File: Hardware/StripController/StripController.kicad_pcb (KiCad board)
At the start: 2 copper layers, 39.6 x 48.3 mm, 49 parts, among them IC1 RY8310, IC2 CH32V003F4U6, J1 Conn_01x03_Socket, J2 Conn_01x06_Socket, J4 Conn_01x02_Pin, J5 TagConnect, J6 Conn_01x03_Socket, Q1 AON7544, Q2 AON7544, Q3 AON7544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

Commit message: edit pcb desine
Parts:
- added C12: 100n, Capacitor_SMD:C_0402_1005Metric, F.Cu at (156.7, 75.7)
- added C13: 100n, Capacitor_SMD:C_0402_1005Metric, F.Cu at (137.8, 59.8)
- added F2: 0,2A, Fuse:Fuse_0402_1005Metric, F.Cu at (155.7, 93.2)
- added R14: 10k, Resistor_SMD:R_0402_1005Metric, F.Cu at (137.2, 93.4)
- added R14: R, Resistor_SMD:R_0402_1005Metric, F.Cu at (155.7, 75.6)
- added R15: 10k, Resistor_SMD:R_0402_1005Metric, F.Cu at (137.1, 86.3)
- added R16: 0, Resistor_SMD:R_0402_1005Metric, B.Cu at (149.9, 98.6)
- added R17: 0, Resistor_SMD:R_0402_1005Metric, B.Cu at (149.9, 100.6)
- added R18: R, Resistor_SMD:R_0402_1005Metric, F.Cu at (156.7, 73.6)
- added R19: 100k, Resistor_SMD:R_0402_1005Metric, F.Cu at (137.8, 57.3)
- added TH1: Thermistor_NTC, Resistor_SMD:R_0402_1005Metric, F.Cu at (137.8, 58.6)
- F1: value Fuse -> 10A
- Q1, Q2, Q3, Q4, Q5: footprint Package_DFN_QFN:DFN-8-1EP_3x3mm_P0.5mm_EP1.65x2.38mm_ThermalVias -> Techbeard:AON7544
- R1: moved to B.Cu
- R7: value NC -> 1k; moved to B.Cu
- moved D4 72.1 mm to (160.8, 50.1), turned to -90 degrees
- moved D3 70.0 mm to (158.8, 50.1), turned to -90 degrees
- moved R13 69.7 mm to (160.8, 52.3), turned to 90 degrees
- moved D2 67.9 mm to (156.8, 50.1), turned to -90 degrees
- moved R12 67.5 mm to (158.8, 52.3), turned to 90 degrees
- moved R1 66.8 mm to (154.7, 99.6)
- moved C6 66.0 mm to (150.0, 78.2), turned to -90 degrees
- moved R11 65.4 mm to (156.8, 52.3), turned to 90 degrees
- moved Q2 65.2 mm to (160.5, 77.2)
- moved R8 64.8 mm to (156.7, 77.7)
- moved C10 64.3 mm to (148.1, 65.1), turned to -90 degrees
- moved R7 62.1 mm to (144.3, 99.6)
- moved C11 62.0 mm to (146.1, 65.1), turned to -90 degrees
- moved D1 60.0 mm to (152.1, 83.3)
- moved R6 59.6 mm to (157.7, 73.7), turned to 90 degrees
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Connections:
- D3 pad 1: StateLed0 -> StateLed1
- D4 pad 1: StateLed1 -> StateLed0
- IC2 pad 10: unconnected-(IC2-PC3-Pad10) -> Voltage
- IC2 pad 11: unconnected-(IC2-PC4-Pad11) -> U2_DE
- IC2 pad 12: unconnected-(IC2-PC5-Pad12) -> U2_RE
- IC2 pad 16: unconnected-(IC2-PD2-Pad16) -> Temp
- IC2 pad 20: U4_RO -> U2_RO
- Q2 pad 4: R -> B
- Q3 pad 4: G -> R
- Q4 pad 4: B -> G
- Q6 pad 3: VCC -> Net-(Q6-D)
- R6 pad 2: G -> R
- R8 pad 2: R -> B
- R9 pad 2: B -> G
- U2 pad 2: +5V -> U2_RE
- U2 pad 3: +5V -> U2_DE
- U4 pad 1: U4_RO -> U2_RO
- U4 pad 2: GND -> Net-(U4-DE)
- U4 pad 3: GND -> Net-(U4-DE)
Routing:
- net +5V: track 0.00 -> 107.8 mm
- net U2_DE: track 0.00 -> 51.6 mm, vias 0 -> 2
- net U2_RE: track 0.00 -> 44.4 mm, vias 0 -> 2
- net U2_DI: track 0.00 -> 43.4 mm, vias 0 -> 2
- net U2_RO: track 0.00 -> 39.9 mm, vias 0 -> 3
- net R: track 0.00 -> 25.7 mm
- net NRST: track 0.00 -> 24.2 mm
- net B: track 0.00 -> 23.9 mm
- net Voltage: track 0.00 -> 22.0 mm
- net RB: track 0.00 -> 21.6 mm
- net G: track 0.00 -> 21.5 mm
- net W: track 0.00 -> 20.8 mm
- net RA: track 0.00 -> 20.0 mm
- net StateLed0: track 0.00 -> 19.9 mm, vias 0 -> 2
- net TB: track 0.00 -> 19.5 mm
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- added copper zone on F.Cu, net +5V
- added copper zone on F.Cu, net B_OUT
- added copper zone on B.Cu, net GND
- added copper zone on F.Cu, net GND
- added copper zone on F.Cu, net Net-(D1-K)
- added copper zone on F.Cu, net Net-(IC1-SW)
- added copper zone on F.Cu, net Net-(J4-Pin_1)
- added copper zone on F.Cu, net R_OUT
- added copper zone on F.Cu, net VCC
- added copper zone on F.Cu, net WW_OUT
- added copper zone on F.Cu, net W_OUT
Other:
- board size 39.6 x 48.3 mm -> 40 x 60 mm

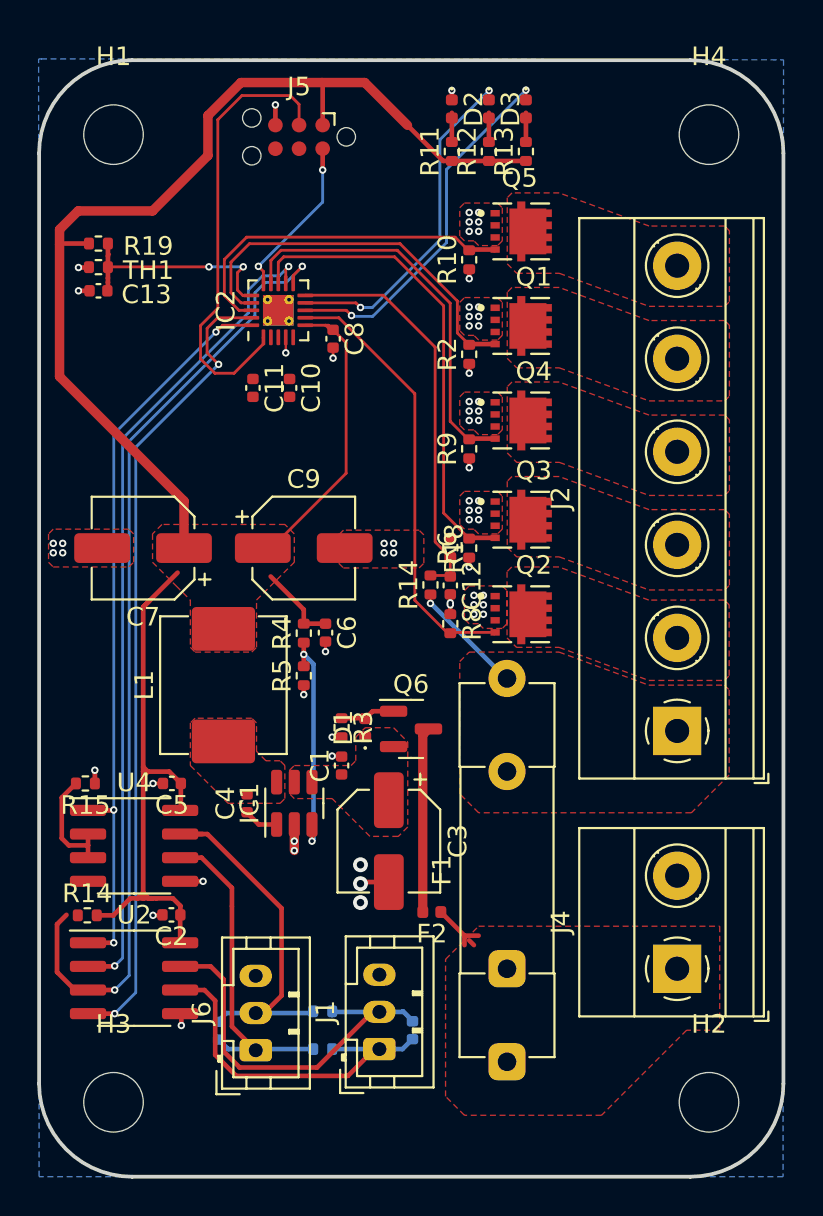
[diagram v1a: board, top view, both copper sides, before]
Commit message: edit Strip controller and buy first batch
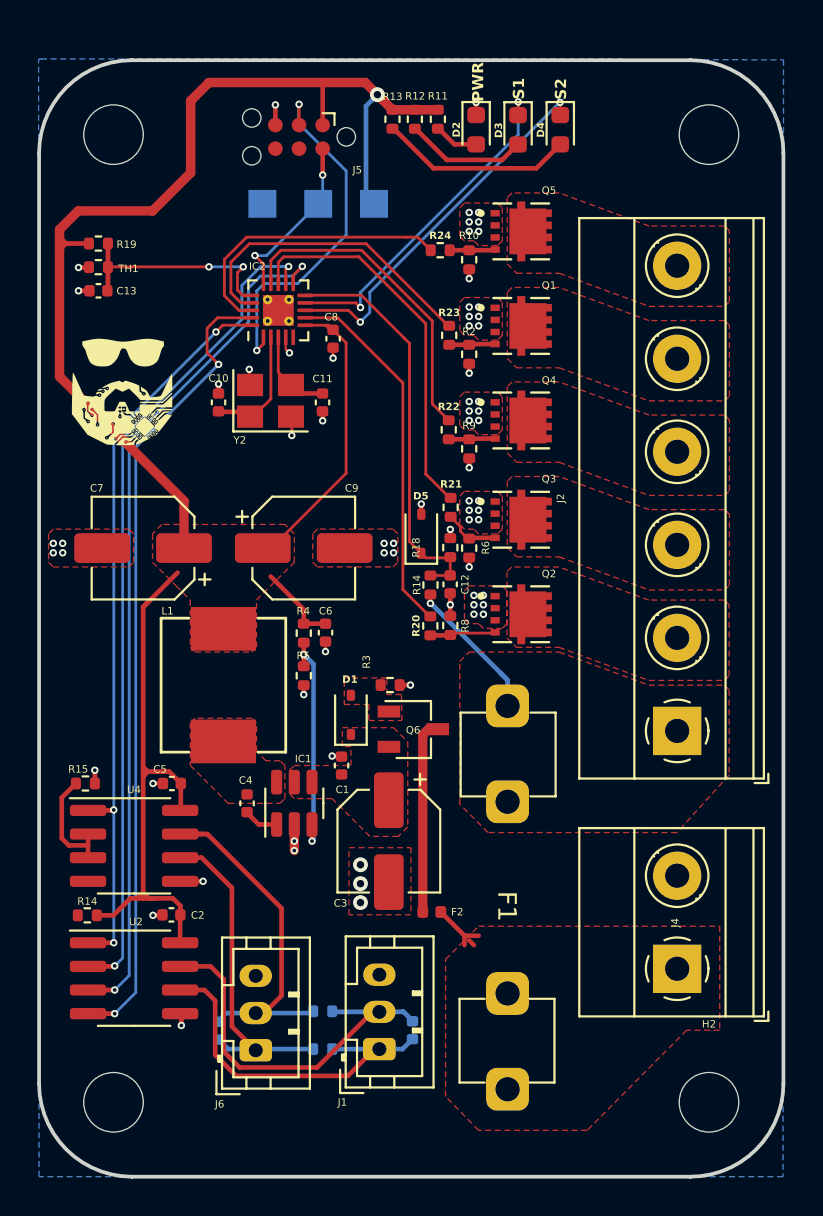
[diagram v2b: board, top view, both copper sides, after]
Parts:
- removed F1: 10A, Fuse:Fuseholder_Clip-5x20mm_Schurter_CQM_Inline_P20.60x5.00mm_D1.00mm_Horizontal
- added D5: 5,1V, Diode_SMD:D_SOD-323, F.Cu at (155.2, 72.9)
- added G***: LOGO, Techbeard:Techbeard_6x6, F.Cu at (139.1, 65.1)
- added G***: LOGO, LOGO, B.Cu at (138.3, 77.4)
- added J10: F1, Techbeard:Fuseholder C3130, F.Cu at (159.8, 84.7)
- added J3: SWD, TestPoint:TestPoint_Pad_1.5x1.5mm, B.Cu at (149.6, 55.2)
- added J7: +5V, TestPoint:TestPoint_Pad_1.5x1.5mm, B.Cu at (152.6, 55.2)
- added J8: GND, TestPoint:TestPoint_Pad_1.5x1.5mm, B.Cu at (146.6, 55.2)
- added J9: F1, Techbeard:Fuseholder C3130, F.Cu at (159.8, 100.2)
- added R20: 47, Resistor_SMD:R_0402_1005Metric, F.Cu at (155.6, 77.8)
- added R21: 47, Resistor_SMD:R_0402_1005Metric, F.Cu at (156.7, 71.5)
- added R22: 47, Resistor_SMD:R_0402_1005Metric, F.Cu at (156.6, 67.3)
- added R23: 47, Resistor_SMD:R_0402_1005Metric, F.Cu at (156.7, 62.2)
- added R24: 47, Resistor_SMD:R_0402_1005Metric, F.Cu at (156.2, 57.7)
- added Y2: Crystal_GND24, Crystal:Crystal_SMD_3225-4Pin_3.2x2.5mm, F.Cu at (147.1, 65.7)
- C3: value 47u -> 22u
- D1: footprint Diode_SMD:D_0402_1005Metric -> Diode_SMD:D_SOD-323
- D2: value LED -> PWR; footprint LED_SMD:LED_0402_1005Metric -> LED_SMD:LED_0603_1608Metric
- D3: value LED -> S1; footprint LED_SMD:LED_0402_1005Metric -> LED_SMD:LED_0603_1608Metric
- D4: value LED -> S2; footprint LED_SMD:LED_0402_1005Metric -> LED_SMD:LED_0603_1608Metric
- L1: footprint Inductor_SMD:L_Abracon_ASPI-0630LR -> Techbeard:L_0630
- Q6: footprint Package_TO_SOT_SMD:SOT-23 -> Package_TO_SOT_SMD:TSOT-23
- R14: value R -> 1M
- R18: value R -> 270k
- moved R13 7.38 mm to (153.6, 50.6), turned to -90 degrees
- moved R12 4.34 mm to (154.8, 50.6), turned to -90 degrees
- moved C10 3.90 mm to (144.3, 65.8), turned to 90 degrees
- moved C11 3.82 mm to (149.9, 65.8)
- moved R3 3.47 mm to (153.5, 81.0), turned to 0 degrees
- moved D4 2.16 mm to (162.6, 51.2)
- moved D3 1.93 mm to (160.4, 51.2)
- moved R11 1.89 mm to (156.0, 50.6), turned to -90 degrees
- moved D2 1.72 mm to (158.1, 51.2)
- moved D1 1.03 mm to (151.4, 82.6)
- moved Q6 0.12 mm to (154.7, 83.4)
- moved R8 0.09 mm to (156.7, 77.8)
- moved C12 0.06 mm to (156.7, 75.6)
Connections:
- IC2 pad 13: R -> G
- IC2 pad 14: G -> B
- IC2 pad 2: (no net) -> Net-(IC2-PA1/OSCI)
- IC2 pad 3: (no net) -> Net-(IC2-PA2/OSCO)
- IC2 pad 7: B -> R
- Q1 pad 4: W -> Net-(Q1-G)
- Q2 pad 4: B -> Net-(Q2-G)
- Q3 pad 4: R -> Net-(Q3-G)
- Q4 pad 4: G -> Net-(Q4-G)
- Q5 pad 4: WW -> Net-(Q5-G)
- R10 pad 2: WW -> Net-(Q5-G)
- R2 pad 2: W -> Net-(Q1-G)
- R6 pad 2: R -> Net-(Q3-G)
- R8 pad 2: B -> Net-(Q2-G)
- R9 pad 2: G -> Net-(Q4-G)
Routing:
- net Net-(D4-A): track 1.57 -> 10.4 mm
- net Net-(IC2-PA1/OSCI): track 0.00 -> 6.62 mm
- net B: track 23.9 -> 17.4 mm
- net R: track 25.7 -> 19.8 mm
- net Net-(D3-A): track 1.57 -> 6.58 mm
- net U2_DE: track 51.6 -> 46.6 mm
- net NRST: track 24.2 -> 19.3 mm, vias 0 -> 2
- net Net-(IC2-PA2/OSCO): track 0.00 -> 4.73 mm
- net W: track 20.8 -> 16.9 mm
- net Net-(Q2-G): track 0.00 -> 3.81 mm
- net WW: track 19.1 -> 15.6 mm
- net GND: track 17.0 -> 20.1 mm, vias 64 -> 69
- net Net-(Q3-G): track 0.00 -> 3.04 mm
- net Net-(D1-A): track 2.97 -> 0.00 mm
- net Net-(Q5-G): track 0.00 -> 2.52 mm
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- added copper zone on F.Cu, net G_OUT
- added copper zone on F.Cu, net Net-(D1-A)
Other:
- board text added: "B"
- board text added: "G"
- board text added: "GND"
- board text added: "R"
- board text added: "Vin"
- board text added: "Vout"
- board text added: "W"
- board text added: "WW"
